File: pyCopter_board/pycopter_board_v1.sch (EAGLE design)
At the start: 17 parts, among them Q1 32.768kHz, U1 BNO055, U3 BMP180

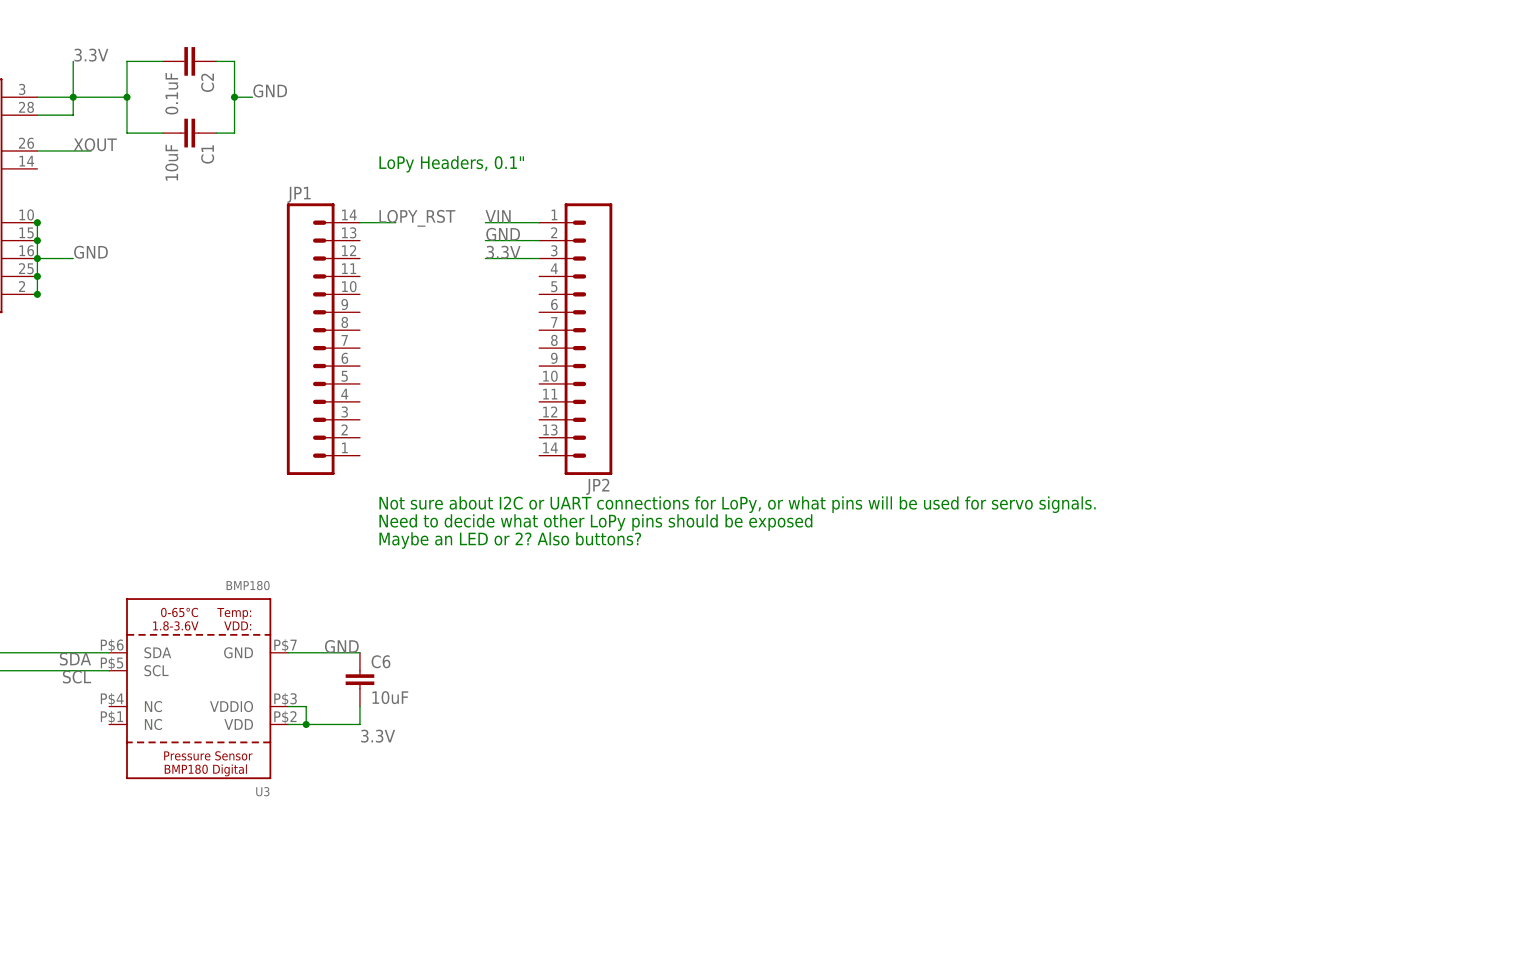
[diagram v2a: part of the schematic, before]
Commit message: modified the pyboard design to include the adafruit ultimate gps module. dropped down some headers for the spektrum transciever module.
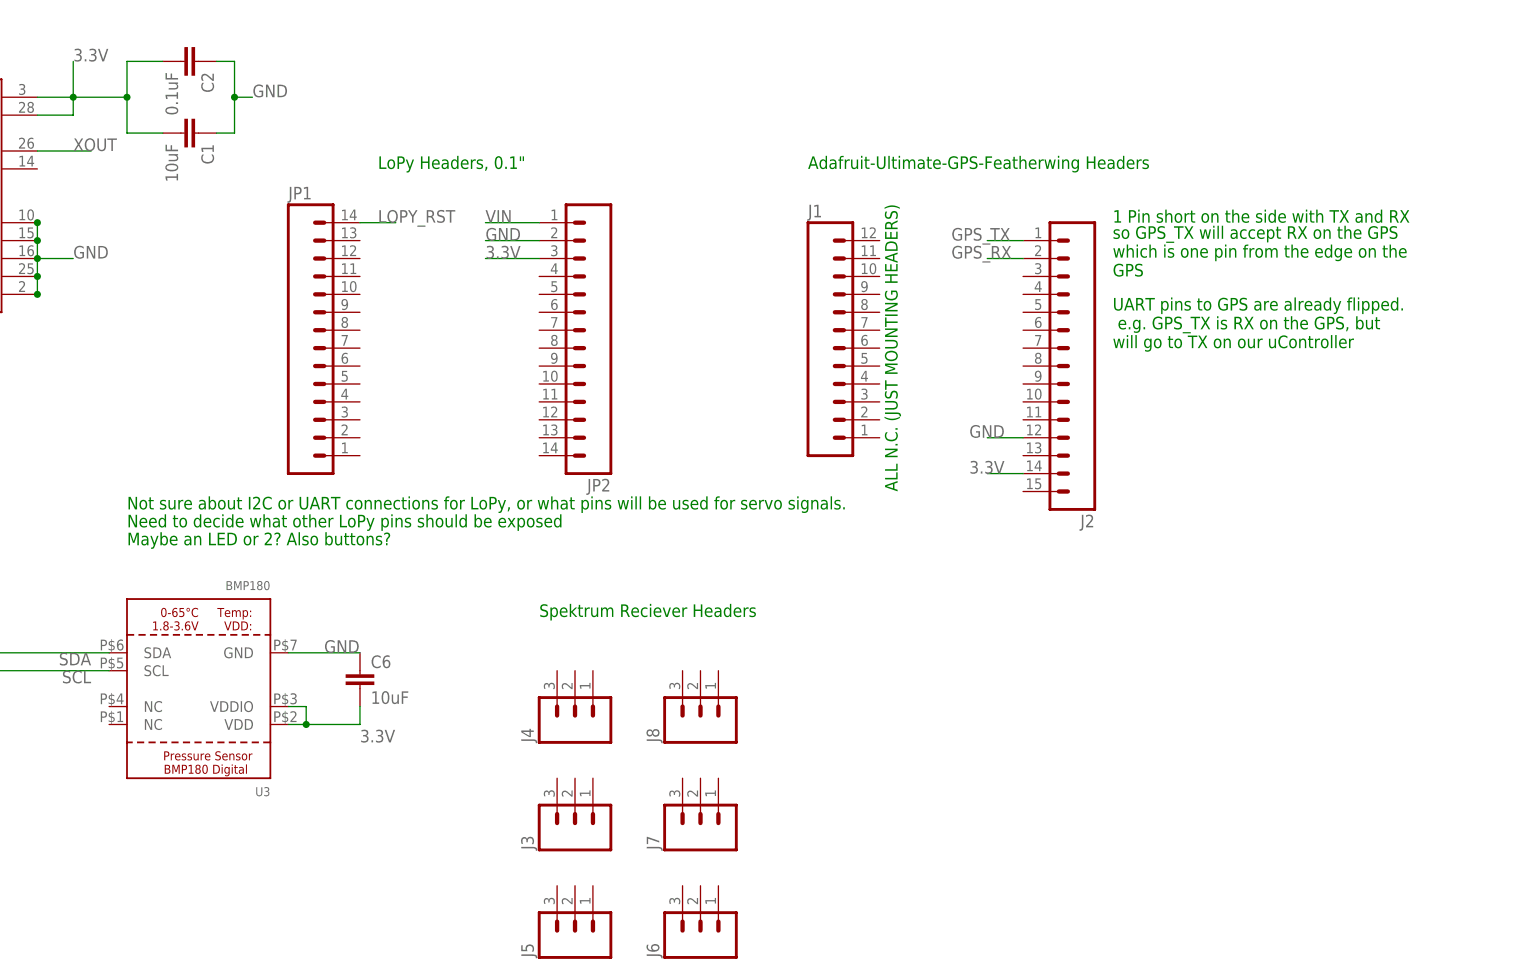
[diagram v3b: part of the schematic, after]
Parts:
- added J1: (no value), SparkFun-Connectors:M12PTH
- added J2: (no value), SparkFun-Connectors:M15
- added J3, J4, J5, J6, J7, J8: (no value), SparkFun-Connectors:M03PTH
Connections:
- new net GPS_RX: J2.2
- new net GPS_TX: J2.1
- net 3.3V: now also J2.14
- net GND: now also J2.12
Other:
- note added: "1 Pin short on the side with TX and RX"
- note added: "ALL N.C. (JUST MOUNTING HEADERS)"
- note added: "Adafruit-Ultimate-GPS-Featherwing Headers"
- note added: "Spektrum Reciever Headers"
- note added: "UART pins to GPS are already flipped. e.g. GPS_TX is RX on the GPS, but will go to TX on our uController"
- note added: "so GPS_TX will accept RX on the GPS which is one pin from the edge on the GPS"
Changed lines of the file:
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@@
 <layer number="112" name="tSilk" color="7" fill="1" visible="no" active="yes"/>
 <layer number="113" name="IDFDebug" color="4" fill="1" visible="no" active="yes"/>
+<layer number="114" name="Badge_Outline" color="7" fill="1" visible="yes" active="yes"/>
+<layer number="115" name="ReferenceISLANDS" color="7" fill="1" visible="yes" active="yes"/>
 <layer number="116" name="Patch_BOT" color="9" fill="4" visible="no" active="yes"/>
 <layer number="118" name="Rect_Pads" color="7" fill="1" visible="yes" active="yes"/>
@@
 <part name="U3" library="microbuilder" deviceset="BMP180" device="EXT" value="BMP180"/>
 <part name="C6" library="SparkFun-Passives" deviceset="CAP" device="0402-CAP" value="10uF"/>
+<part name="J1" library="SparkFun-Connectors" deviceset="M12" device="PTH"/>
+<part name="J2" library="SparkFun-Connectors" deviceset="M15" device=""/>
+<part name="J3" library="SparkFun-Connectors" deviceset="M03" device="PTH"/>
+<part name="J4" library="SparkFun-Connectors" deviceset="M03" device="PTH"/>
+<part name="J5" library="SparkFun-Connectors" deviceset="M03" device="PTH"/>
+<part name="J6" library="SparkFun-Connectors" deviceset="M03" device="PTH"/>
+<part name="J7" library="SparkFun-Connectors" deviceset="M03" device="PTH"/>
+<part name="J8" library="SparkFun-Connectors" deviceset="M03" device="PTH"/>
 </parts>
 <sheets>
@@
 <plain>
 <text x="63.5" y="71.12" size="1.778" layer="91">LoPy Headers, 0.1"</text>
-<text x="63.5" y="22.86" size="1.778" layer="91">Not sure about I2C or UART connections for LoPy, or what pins will be used for servo signals.  </text>
-<text x="63.5" y="20.32" size="1.778" layer="91">Need to decide what other LoPy pins should be exposed </text>
-<text x="63.5" y="17.78" size="1.778" layer="91">Maybe an LED or 2? Also buttons?</text>
+<text x="27.94" y="22.86" size="1.778" layer="91">Not sure about I2C or UART connections for LoPy, or what pins will be used for servo signals.  </text>
+<text x="27.94" y="20.32" size="1.778" layer="91">Need to decide what other LoPy pins should be exposed </text>
+<text x="27.94" y="17.78" size="1.778" layer="91">Maybe an LED or 2? Also buttons?</text>
+<text x="124.46" y="71.12" size="1.778" layer="91">Adafruit-Ultimate-GPS-Featherwing Headers</text>
+<text x="167.64" y="63.5" size="1.778" layer="91">1 Pin short on the side with TX and RX</text>
+<text x="167.64" y="45.72" size="1.778" layer="91">UART pins to GPS are already flipped.
+ e.g. GPS_TX is RX on the GPS, but
+will go to TX on our uController</text>
+<text x="167.64" y="55.88" size="1.778" layer="91">so GPS_TX will accept RX on the GPS
+which is one pin from the edge on the
+GPS</text>
+<text x="137.16" y="25.4" size="1.778" layer="91" rot="R90">ALL N.C. (JUST MOUNTING HEADERS)</text>
+<text x="86.36" y="7.62" size="1.778" layer="91">Spektrum Reciever Headers</text>
 </plain>
 <instances>
@@
 <instance part="U3" gate="G$1" x="38.1" y="-2.54" rot="R180"/>
 <instance part="C6" gate="G$1" x="60.96" y="-2.54"/>
+<instance part="J1" gate="G$1" x="124.46" y="48.26"/>
+<instance part="J2" gate="G$1" x="165.1" y="43.18" rot="R180"/>
+<instance part="J3" gate="J$1" x="91.44" y="-22.86" rot="R90"/>
+<instance part="J4" gate="J$1" x="91.44" y="-7.62" rot="R90"/>
+<instance part="J5" gate="J$1" x="91.44" y="-38.1" rot="R90"/>
+<instance part="J6" gate="J$1" x="109.22" y="-38.1" rot="R90"/>
+<instance part="J7" gate="J$1" x="109.22" y="-22.86" rot="R90"/>
+<instance part="J8" gate="J$1" x="109.22" y="-7.62" rot="R90"/>
 </instances>
 <busses>
@@
 <pinref part="C6" gate="G$1" pin="1"/>
 </segment>
+<segment>
+<pinref part="J2" gate="G$1" pin="12"/>
+<wire x1="154.94" y1="33.02" x2="149.86" y2="33.02" width="0.1524" layer="91"/>
+<label x="147.32" y="33.02" size="1.778" layer="95"/>
+</segment>
 </net>
 <net name="3.3V" class="0">
@@
 <label x="60.96" y="-10.16" size="1.778" layer="95"/>
 </segment>
+<segment>
+<pinref part="J2" gate="G$1" pin="14"/>
+<wire x1="154.94" y1="27.94" x2="149.86" y2="27.94" width="0.1524" layer="91"/>
+<label x="147.32" y="27.94" size="1.778" layer="95"/>
+</segment>
 </net>
 <net name="LOPY_RST" class="0">
@@
 </segment>
 </net>
+<net name="GPS_TX" class="0">
+<segment>
+<pinref part="J2" gate="G$1" pin="1"/>
+<wire x1="154.94" y1="60.96" x2="149.86" y2="60.96" width="0.1524" layer="91"/>
+<label x="144.78" y="60.96" size="1.778" layer="95"/>
+</segment>
+</net>
+<net name="GPS_RX" class="0">
+<segment>
+<pinref part="J2" gate="G$1" pin="2"/>
+<wire x1="154.94" y1="58.42" x2="149.86" y2="58.42" width="0.1524" layer="91"/>
+<label x="144.78" y="58.42" size="1.778" layer="95"/>
+</segment>
+</net>
 </nets>
 </sheet>
@@
 </schematic>
 </drawing>
+<compatibility>
+<note version="6.3" minversion="6.2.2" severity="warning">
+Since Version 6.2.2 text objects can contain more than one line,
+which will not be processed correctly with this version.
+</note>
+</compatibility>
 </eagle>

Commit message: added gps tx and rx connections to LoPy board, began determining the pin definitions of LoPy board.
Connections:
- net GPS_RX: now also JP1.9
- net GPS_TX: now also JP1.10
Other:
- note added: "Connect to external interrupt pins on LoPy"
- note added: "LoPy LED"
- note added: "N.C."
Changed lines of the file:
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@@
 <text x="137.16" y="25.4" size="1.778" layer="91" rot="R90">ALL N.C. (JUST MOUNTING HEADERS)</text>
 <text x="86.36" y="7.62" size="1.778" layer="91">Spektrum Reciever Headers</text>
+<text x="78.74" y="5.08" size="1.778" layer="91">Connect to external interrupt pins on LoPy</text>
+<text x="60.96" y="48.26" size="1.778" layer="91">N.C.</text>
+<text x="60.96" y="45.72" size="1.778" layer="91">N.C.</text>
+<text x="60.96" y="43.18" size="1.778" layer="91">N.C.</text>
+<text x="60.96" y="55.88" size="1.778" layer="91">LoPy LED</text>
 </plain>
 <instances>
@@
 <label x="144.78" y="60.96" size="1.778" layer="95"/>
 </segment>
+<segment>
+<pinref part="JP1" gate="G$1" pin="10"/>
+<wire x1="60.96" y1="53.34" x2="66.04" y2="53.34" width="0.1524" layer="91"/>
+<label x="60.96" y="53.34" size="1.778" layer="95"/>
+</segment>
 </net>
 <net name="GPS_RX" class="0">
@@
 <label x="144.78" y="58.42" size="1.778" layer="95"/>
 </segment>
-</net>
+<segment>
+<pinref part="JP1" gate="G$1" pin="9"/>
+<wire x1="60.96" y1="50.8" x2="66.04" y2="50.8" width="0.1524" layer="91"/>
+<label x="60.96" y="50.8" size="1.778" layer="95"/>
+</segment>
+</net>

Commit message: Added boarded files
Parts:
- added BMP180BREAK: (no value), SparkFun-Connectors:M05PTH
- added ESC1, ESC2, ESC3, ESC4: (no value), SparkFun-Connectors:M02PTH
- added EXTRALOPYHEAD: (no value), SparkFun-Connectors:M08SILK_FEMALE_PTH
- added H5, H6, H7, H8: MOUNT-HOLE3.0, holes:MOUNT-HOLE3.0
- added IMUBREAK: (no value), SparkFun-Connectors:M06SILK_FEMALE_PTH
- renumbered J1 to GPSLEFT, J2 to GPSRIGHT, JP1 to LOPYLEFT, JP2 to LOPYRIGHT
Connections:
- new net AILE: J4.1, LOPYLEFT.2
- new net AUX1: J8.1, LOPYRIGHT.6
- new net ELEV: J5.1, LOPYLEFT.1
- new net GEAR: J7.1, LOPYRIGHT.12
- new net N$7: BMP180BREAK.4
- new net N$9: LOPYRIGHT.9
- new net P0: EXTRALOPYHEAD.2, LOPYLEFT.13
- new net P17: EXTRALOPYHEAD.1, LOPYRIGHT.10
- new net P19: ESC1.2, LOPYRIGHT.8
- new net P20: ESC2.2, LOPYRIGHT.7
- new net P22: ESC4.2, EXTRALOPYHEAD.3, LOPYRIGHT.5
- new net P23: ESC3.2, EXTRALOPYHEAD.4, LOPYRIGHT.4
- new net RUDD: J6.1, LOPYRIGHT.11
- new net THRO: J3.1, LOPYLEFT.5
- net 3.3V: now also BMP180BREAK.5, EXTRALOPYHEAD.8, IMUBREAK.6, J3.2
- net GND: now also BMP180BREAK.3, ESC1.1, ESC2.1, ESC3.1, ESC4.1, EXTRALOPYHEAD.7, IMUBREAK.4, J3.3
- net SCL: now also BMP180BREAK.2, EXTRALOPYHEAD.6, IMUBREAK.2, LOPYLEFT.3
- net SDA: now also BMP180BREAK.1, EXTRALOPYHEAD.5, IMUBREAK.3, LOPYLEFT.4
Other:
- note added: "Breakout headers just in case"
